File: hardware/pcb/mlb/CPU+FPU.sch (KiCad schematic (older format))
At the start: 5 parts, among them J13 PDS_03x80

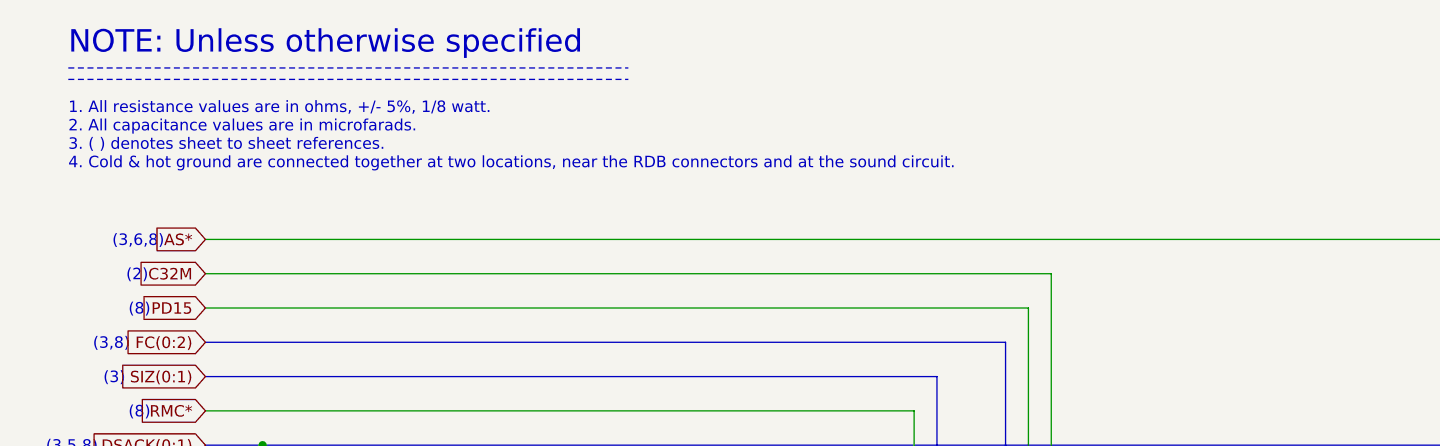
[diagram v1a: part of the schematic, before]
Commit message: Fix typos ADB, PAL16L8D.
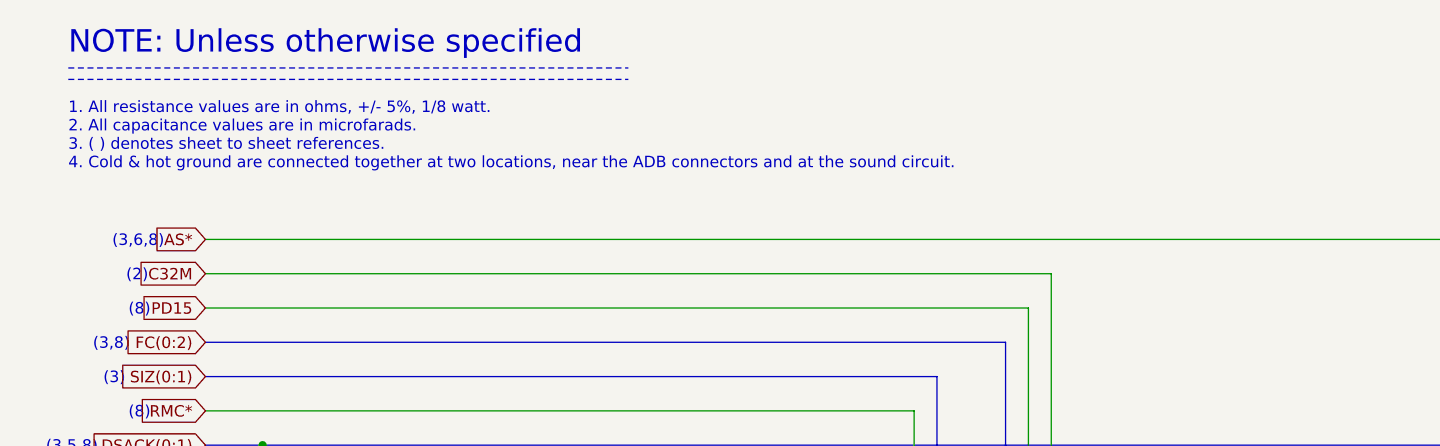
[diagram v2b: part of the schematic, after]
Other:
- note added: "1. All resistance values are in ohms, +/- 5%, 1/8 watt.\n2. All capacitance values are in microfarads.\n3. ( ) denotes sheet to sheet references.\n4. Cold & hot ground are connected together at two locations, near the ADB connectors and at the sound circuit."
- note removed: "1. All resistance values are in ohms, +/- 5%, 1/8 watt.\n2. All capacitance values are in microfarads.\n3. ( ) denotes sheet to sheet references.\n4. Cold & hot ground are connected together at two locations, near the RDB connectors and at the sound circuit."
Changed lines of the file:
@@
 	700  900  3150 900
 Text Notes 700  1300 0    50   ~ 0
-1. All resistance values are in ohms, +/- 5%, 1/8 watt.\n2. All capacitance values are in microfarads.\n3. ( ) denotes sheet to sheet references.\n4. Cold & hot ground are connected together at two locations, near the RDB connectors and at the sound circuit.
+1. All resistance values are in ohms, +/- 5%, 1/8 watt.\n2. All capacitance values are in microfarads.\n3. ( ) denotes sheet to sheet references.\n4. Cold & hot ground are connected together at two locations, near the ADB connectors and at the sound circuit.
 Wire Wire Line
 	11550 2200 11550 3650

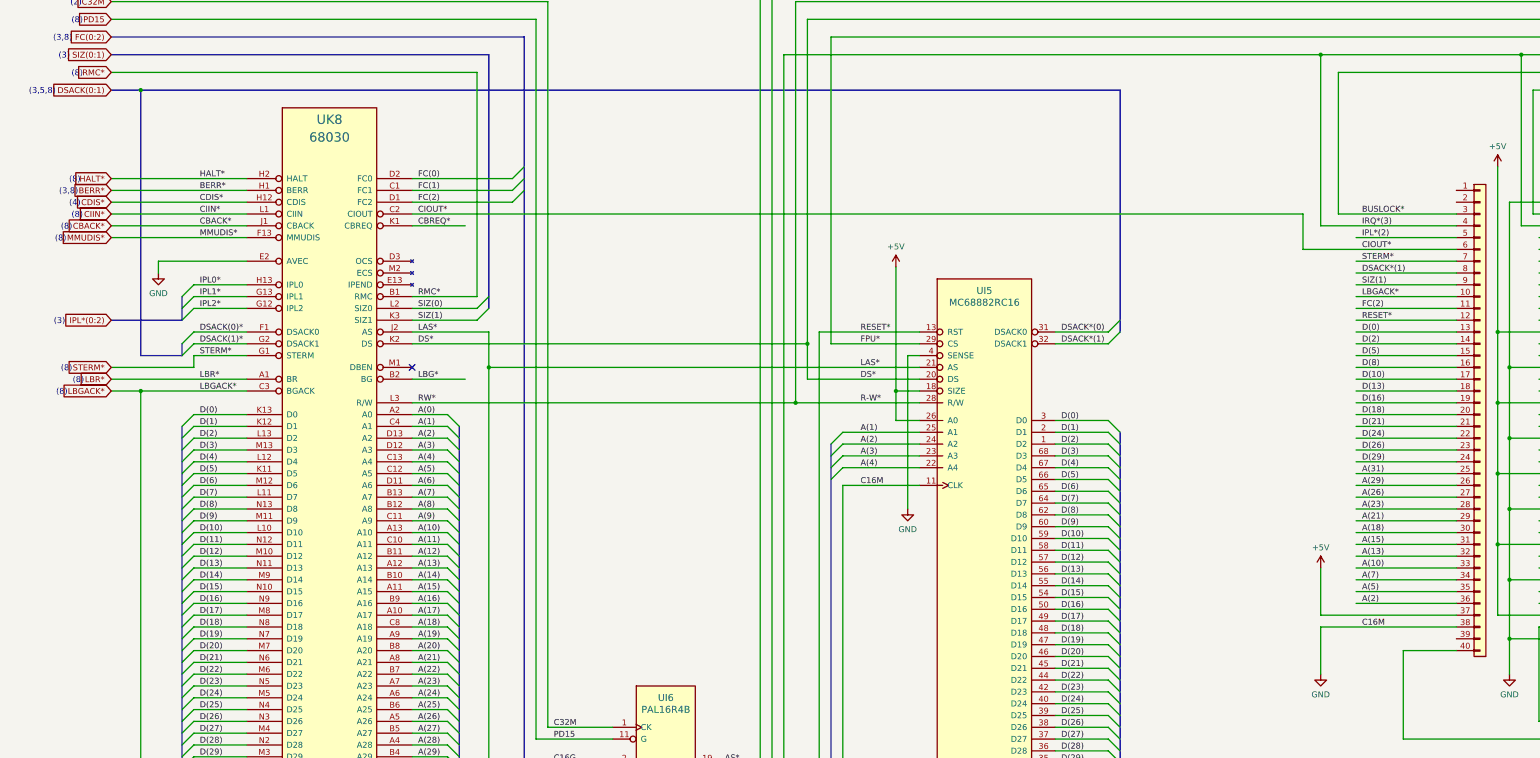
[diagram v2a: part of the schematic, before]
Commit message: Fix errors found in review of the Macintosh SE/30 schematic redraw.
Page 1:

* DSACK*(0:1) (syntax)
* R-W* (inconsistent syntax)
* IPL different syntax
* PDS 38, C16M not grounded
* PDS 39, should be grounded

Page 2:

* RAAF*(8), RABF*(9), RAAF*(10), RABF*(10) (syntax)
* RCMUX* (syntax)
* ROM* missing page 3 indicator
* ROMSIMM1 GND 10, 30, 64
* ROMSIMM1 Incorrect +5V lines
* ROMSIMM1 Confusing bus line drawing angles makes connections look
  duplicated

Page 3:

* VIAIRQ2* (syntax)
* VIAIRQ1N (syntax, on GLUE template)
* SCCRD* (syntax)

Page 4:

* VIA template, RS0, RS1, RS2, RS3 erroneously written as R50, R51,
  R52, R53
* V1PB7 erroneously written as VIPB7
* RTC-D erroneously written as RTC-O
* V1PA0, V1PA1, V1PA2 erroneously written as VIPA0, VIPA1, VIPA2
* warning: additional label BATT not present
* UL11 ADB template, P5 erroneously written as P2
* ADBO erroneously written as ADB0
* SNDINT* erroneously written as SNTINT*

Page 5:

* HSYNC* on UG7 (syntax)
* UJ6 confusing bus line makes signals look duplicated
* Video ROM UK6 not labeled with reference designator (already inside
  KiCad file, stale PDF?)
* VIDS4, VIDS3, VIDS2, VIDS1, VIDS0 erroneously written a VID54,
  VID53, VID53, VID51, VID50
* R-W* alternate page reference erroneously written as RW*
* 74F253 template, G erroneously labeled as GND
* 74F253 template, missing second G enable pin
* style: C0 in 74F253 template should not be C0(GND)
* warning: UA8 ALTVID line could have another label close to the chip

Page 6:

* warning: On SWIM, WRDATA could have label WR*
* DB25 connector: DP*, DB0*, DB1*, DB2*, DB3*, DB4*, DB5*, DB6*, DB7*
  (syntax)
* J8 Ribbon Connector: Missing +12V on 13, 15, 17, 19
* J6 DB-19: Missing +12V-DSK on 7, 8
* warning: missing RDDATA.F additional label near J6 DB-19 pin 18
* warning: missing WRITE.F additional label near J6 DB-19 pin 19
* warning: confusing bus line layout on 53C80 looks like duplicate
  wiring

Page 7:

* RXDA+ erroneously written as RXDB+
* HSKOA erroneo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
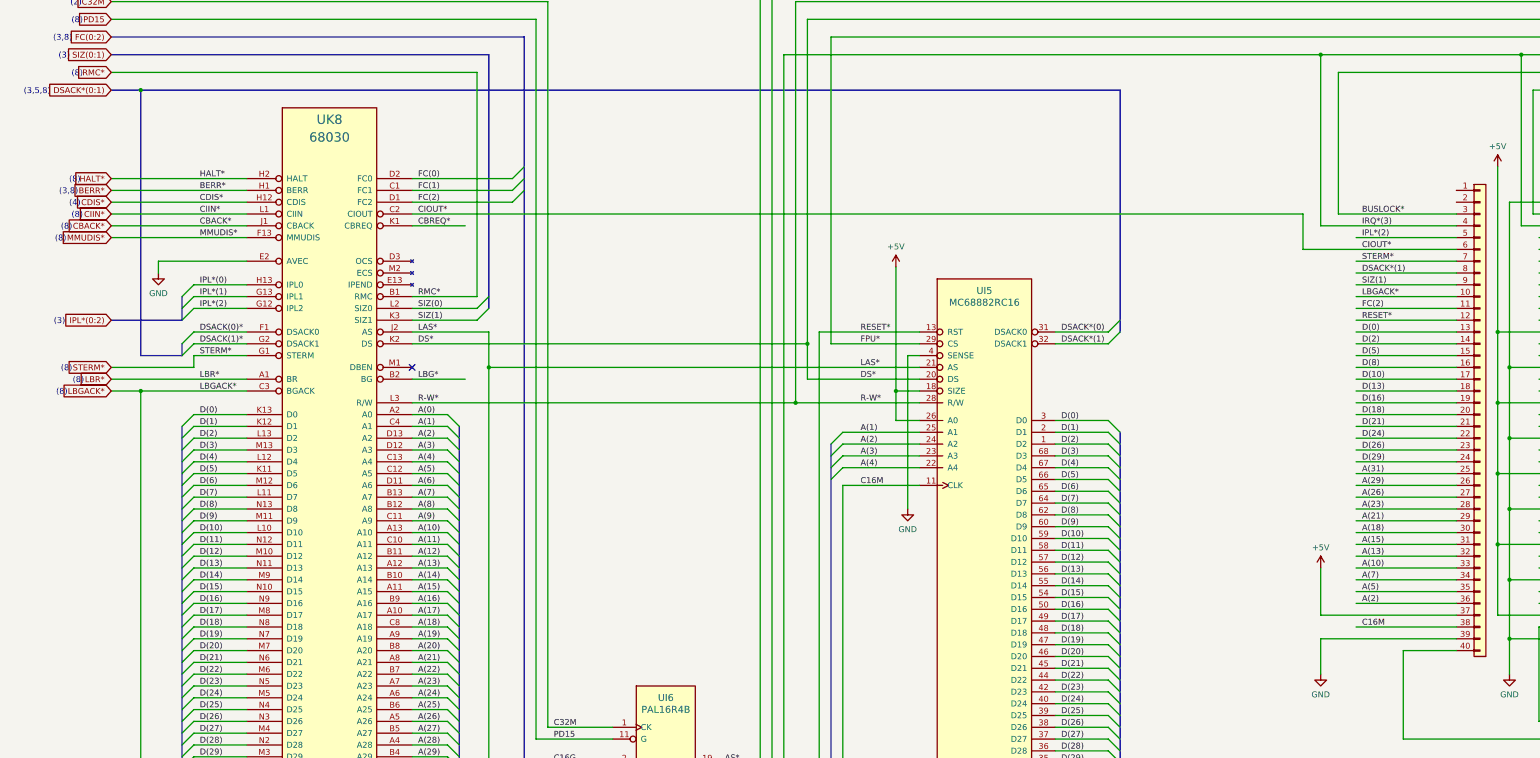
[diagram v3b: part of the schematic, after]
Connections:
- net labels added: DSACK*(0:1)
- net labels removed: DSACK(0:1), IPL0*, IPL1*, IPL2*, RW*
- wire segments 361 -> 362
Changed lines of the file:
@@
 MMUDIS*
 Text Label 2050 4350 0    50   ~ 0
-IPL2*
+IPL*(2)
 Text Label 2050 4250 0    50   ~ 0
-IPL1*
+IPL*(1)
 Text Label 2050 4150 0    50   ~ 0
-IPL0*
+IPL*(0)
 Wire Wire Line
 	2000 4150 2450 4150
@@
 	1700 3950 2450 3950
 Text GLabel 1300 2500 0    50   Input ~ 0
-DSACK(0:1)
+DSACK*(0:1)
 Text GLabel 1300 4850 0    50   Input ~ 0
 STERM*
@@
 $EndComp
 Wire Wire Line
-	11550 7050 11550 7450
-Wire Wire Line
-	11550 7050 12700 7050
+	11850 7050 12700 7050
 $Comp
 L power:GND #PWR?
@@
 Text Label 3900 4950 0    50   ~ 0
 LBG*
-Text Label 3900 5150 0    50   ~ 0
-RW*
 Text Label 3900 5250 0    50   ~ 0
 A(0)
@@
 Text Notes 1040 3290 2    50   ~ 0
 (8)
-Text Notes 830  2540 2    50   ~ 0
-(3,5,8)
 Text Notes 1060 2390 2    50   ~ 0
 (8)
@@
 Text Notes 1120 1640 2    50   ~ 0
 (3,6,8)
+Text Notes 786  2541 2    50   ~ 0
+(3,5,8)
+Wire Wire Line
+	12700 7150 11550 7150
+Wire Wire Line
+	11550 7150 11550 7450
 Wire Bus Line
 	4500 2200 4500 4350
@@
 Wire Bus Line
 	4250 5350 4250 10000
+Text Label 3900 5150 0    50   ~ 0
+R-W*
 $EndSCHEMATC

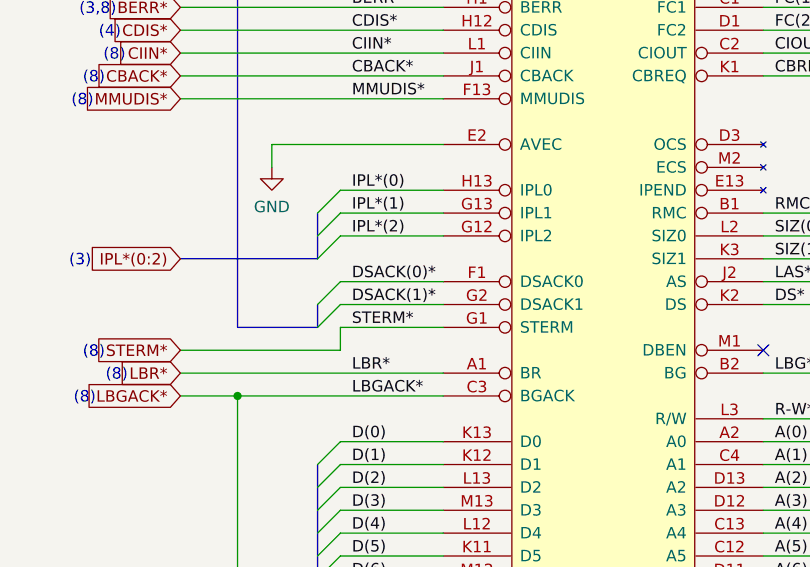
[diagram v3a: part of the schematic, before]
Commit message: Fix some minor errors found from review of desired changes.
* DSACK*(0:1) (syntax)

* Wires wrong on redraw of 74F253 template.
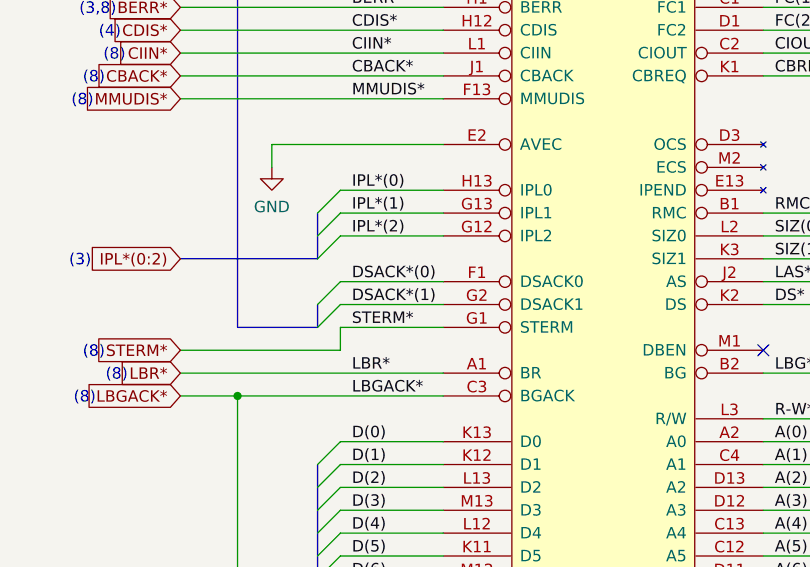
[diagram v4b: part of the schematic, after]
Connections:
- net labels removed: DSACK(0)*, DSACK(1)*
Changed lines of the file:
@@
 	14650 2200 15800 2200
 Text Label 2050 4550 0    50   ~ 0
-DSACK(0)*
+DSACK*(0)
 Text Label 2050 4650 0    50   ~ 0
-DSACK(1)*
+DSACK*(1)
 Text Label 2050 4750 0    50   ~ 0
 STERM*
@@
 Wire Wire Line
 	11550 7150 11550 7450
+Text Label 3900 5150 0    50   ~ 0
+R-W*
 Wire Bus Line
 	4500 2200 4500 4350
@@
 Wire Bus Line
 	4250 5350 4250 10000
-Text Label 3900 5150 0    50   ~ 0
-R-W*
 $EndSCHEMATC
